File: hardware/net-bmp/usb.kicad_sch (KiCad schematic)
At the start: 8 parts, among them J1 USB_C_Receptacle_USB2.0, U2 USBLC6-2SC6

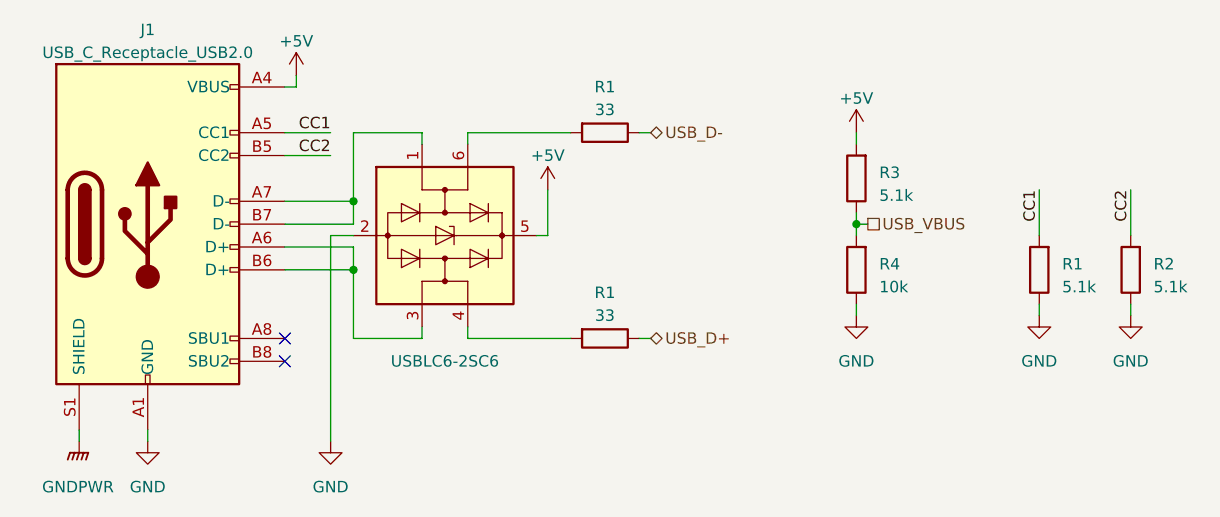
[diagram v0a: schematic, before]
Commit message: chore: build with stubs
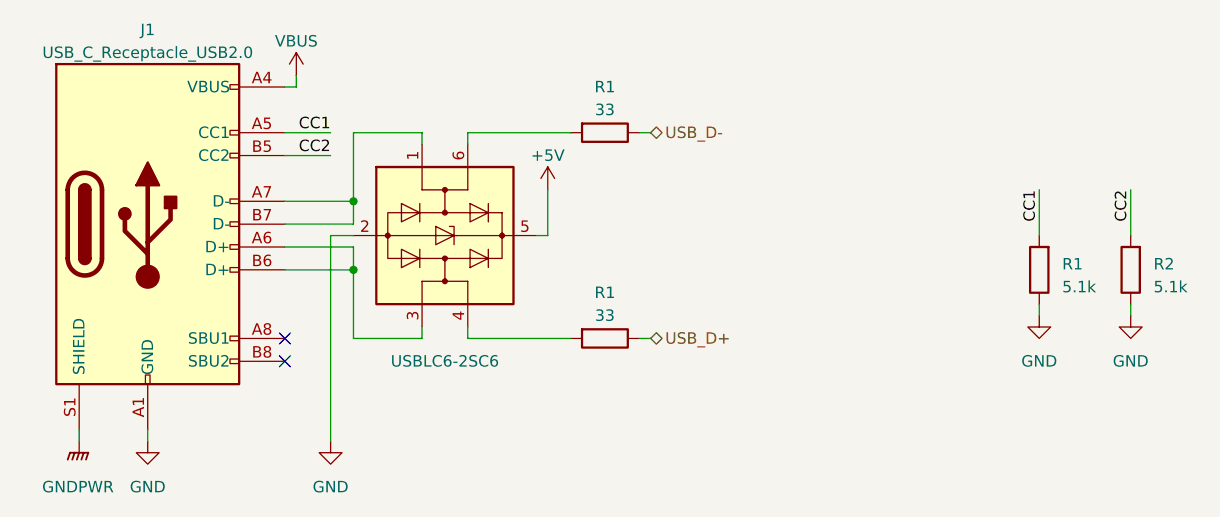
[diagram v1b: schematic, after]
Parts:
- removed R3: 5.1k, Resistor_SMD:R_0402_1005Metric, symbol Device:R
- removed R4: 10k, Resistor_SMD:R_0402_1005Metric, symbol Device:R
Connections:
- net +5V: no longer J1.A4 (VBUS), J1.A9 (VBUS), J1.B4 (VBUS), J1.B9 (VBUS)
- new net VBUS: J1.A4 (VBUS), J1.A9 (VBUS), J1.B4 (VBUS), J1.B9 (VBUS)
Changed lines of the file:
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@@
   (title_block
     (title "net-bmp")
-    (date "2023-10-31")
-    (rev "a")
+    (date "2023-11-11")
+    (rev "b")
     (company "elagil")
-  )
-  (junction (at 119.38 46.99) (diameter 0) (color 0 0 0 0)
   )
   (junction (at 63.5 44.45) (diameter 0) (color 0 0 0 0)
@@
     (stroke (width 0) (type default))
   )
-  (wire (pts (xy 119.38 36.83) (xy 119.38 38.1))
-    (stroke (width 0) (type default))
-  )
   (wire (pts (xy 149.86 55.88) (xy 149.86 57.15))
     (stroke (width 0) (type default))
@@
     (stroke (width 0) (type default))
   )
-  (wire (pts (xy 119.38 45.72) (xy 119.38 46.99))
-    (stroke (width 0) (type default))
-  )
   (wire (pts (xy 95.25 59.69) (xy 96.52 59.69))
     (stroke (width 0) (type default))
@@
     (stroke (width 0) (type default))
   )
-  (wire (pts (xy 119.38 46.99) (xy 119.38 48.26))
-    (stroke (width 0) (type default))
-  )
   (wire (pts (xy 55.88 31.75) (xy 57.15 31.75))
     (stroke (width 0) (type default))
   )
-  (wire (pts (xy 119.38 55.88) (xy 119.38 57.15))
-    (stroke (width 0) (type default))
-  )
   (wire (pts (xy 55.88 49.53) (xy 63.5 49.53))
-    (stroke (width 0) (type default))
-  )
-  (wire (pts (xy 119.38 46.99) (xy 120.65 46.99))
     (stroke (width 0) (type default))
   )
@@
     (effects (font (size 1.27 1.27)) (justify right bottom))
   )
-  (hierarchical_label "USB_VBUS" (shape passive) (at 120.65 46.99 0) (fields_autoplaced)
-    (effects (font (size 1.27 1.27)) (justify left))
-  )
   (hierarchical_label "USB_D+" (shape bidirectional) (at 96.52 59.69 0) (fields_autoplaced)
     (effects (font (size 1.27 1.27)) (justify left))
@@
   (hierarchical_label "USB_D-" (shape bidirectional) (at 96.52 36.83 0) (fields_autoplaced)
     (effects (font (size 1.27 1.27)) (justify left))
+  )
+  (symbol (lib_id "power:VBUS") (at 57.15 30.48 0) (unit 1)
+    (in_bom yes) (on_board yes) (dnp no)
+    (property "Reference" "#PWR067" (at 57.15 34.29 0)
+      (effects (font (size 1.27 1.27)) hide)
+    )
+    (property "Value" "VBUS" (at 57.15 26.67 0)
+      (effects (font (size 1.27 1.27)))
+    )
+    (property "Footprint" "" (at 57.15 30.48 0)
+      (effects (font (size 1.27 1.27)) hide)
+    )
+    (property "Datasheet" "" (at 57.15 30.48 0)
+      (effects (font (size 1.27 1.27)) hide)
+    )
+    (pin "1")
+    (instances
+      (project "net-bmp"
+        (path "/0556e588-02fe-48e5-93e8-fa3aab1c90e7/e157d64e-477b-4983-afb5-0491664aa612"
+          (reference "#PWR067") (unit 1)
+        )
+      )
+    )
   )
   (symbol (lib_id "Connector:USB_C_Receptacle_USB2.0") (at 40.64 46.99 0) (unit 1)
@@
     )
   )
-  (symbol (lib_id "power:+5V") (at 57.15 30.48 0) (unit 1)
-    (in_bom yes) (on_board yes) (dnp no) (fields_autoplaced)
-    (property "Reference" "#PWR08" (at 57.15 34.29 0)
-      (effects (font (size 1.27 1.27)) hide)
-    )
-    (property "Value" "+5V" (at 57.15 26.67 0)
-      (effects (font (size 1.27 1.27)))
-    )
-    (property "Footprint" "" (at 57.15 30.48 0)
-      (effects (font (size 1.27 1.27)) hide)
-    )
-    (property "Datasheet" "" (at 57.15 30.48 0)
-      (effects (font (size 1.27 1.27)) hide)
-    )
-    (pin "1")
-    (instances
-      (project "net-bmp"
-        (path "/0556e588-02fe-48e5-93e8-fa3aab1c90e7"
-          (reference "#PWR08") (unit 1)
-        )
-        (path "/0556e588-02fe-48e5-93e8-fa3aab1c90e7/e157d64e-477b-4983-afb5-0491664aa612"
-          (reference "#PWR064") (unit 1)
-        )
-      )
-    )
-  )
-  (symbol (lib_id "Device:R") (at 119.38 41.91 180) (unit 1)
-    (in_bom yes) (on_board yes) (dnp no) (fields_autoplaced)
-    (property "Reference" "R3" (at 121.92 41.275 0)
-      (effects (font (size 1.27 1.27)) (justify right))
-    )
-    (property "Value" "5.1k" (at 121.92 43.815 0)
-      (effects (font (size 1.27 1.27)) (justify right))
-    )
-    (property "Footprint" "Resistor_SMD:R_0402_1005Metric" (at 121.158 41.91 90)
-      (effects (font (size 1.27 1.27)) hide)
-    )
-    (property "Datasheet" "~" (at 119.38 41.91 0)
-      (effects (font (size 1.27 1.27)) hide)
-    )
-    (property "MPN" "C25905" (at 119.38 41.91 0)
-      (effects (font (size 1.27 1.27)) hide)
-    )
-    (property "JLCPCB Rotation Offset" "" (at 119.38 41.91 0)
-      (effects (font (size 1.27 1.27)) hide)
-    )
-    (pin "1")
-    (pin "2")
-    (instances
-      (project "net-bmp"
-        (path "/0556e588-02fe-48e5-93e8-fa3aab1c90e7"
-          (reference "R3") (unit 1)
-        )
-        (path "/0556e588-02fe-48e5-93e8-fa3aab1c90e7/e157d64e-477b-4983-afb5-0491664aa612"
-          (reference "R31") (unit 1)
-        )
-      )
-    )
-  )
-  (symbol (lib_id "Device:R") (at 119.38 52.07 180) (unit 1)
-    (in_bom yes) (on_board yes) (dnp no) (fields_autoplaced)
-    (property "Reference" "R4" (at 121.92 51.435 0)
-      (effects (font (size 1.27 1.27)) (justify right))
-    )
-    (property "Value" "10k" (at 121.92 53.975 0)
-      (effects (font (size 1.27 1.27)) (justify right))
-    )
-    (property "Footprint" "Resistor_SMD:R_0402_1005Metric" (at 121.158 52.07 90)
-      (effects (font (size 1.27 1.27)) hide)
-    )
-    (property "Datasheet" "~" (at 119.38 52.07 0)
-      (effects (font (size 1.27 1.27)) hide)
-    )
-    (property "MPN" "C25744" (at 119.38 52.07 0)
-      (effects (font (size 1.27 1.27)) hide)
-    )
-    (property "JLCPCB Rotation Offset" "" (at 119.38 52.07 0)
-      (effects (font (size 1.27 1.27)) hide)
-    )
-    (pin "1")
-    (pin "2")
-    (instances
-      (project "net-bmp"
-        (path "/0556e588-02fe-48e5-93e8-fa3aab1c90e7"
-          (reference "R4") (unit 1)
-        )
-        (path "/0556e588-02fe-48e5-93e8-fa3aab1c90e7/e157d64e-477b-4983-afb5-0491664aa612"
-          (reference "R32") (unit 1)
-        )
-      )
-    )
-  )
   (symbol (lib_id "power:GNDPWR") (at 33.02 71.12 0) (unit 1)
     (in_bom yes) (on_board yes) (dnp no) (fields_autoplaced)
@@
         )
       )
-    )
-  )
-  (symbol (lib_id "power:+5V") (at 119.38 36.83 0) (unit 1)
-    (in_bom yes) (on_board yes) (dnp no) (fields_autoplaced)
-    (property "Reference" "#PWR013" (at 119.38 40.64 0)
-      (effects (font (size 1.27 1.27)) hide)
-    )
-    (property "Value" "+5V" (at 119.38 33.02 0)
-      (effects (font (size 1.27 1.27)))
-    )
-    (property "Footprint" "" (at 119.38 36.83 0)
-      (effects (font (size 1.27 1.27)) hide)
-    )
-    (property "Datasheet" "" (at 119.38 36.83 0)
-      (effects (font (size 1.27 1.27)) hide)
-    )
-    (pin "1")
-    (instances
-      (project "net-bmp"
-        (path "/0556e588-02fe-48e5-93e8-fa3aab1c90e7"
-          (reference "#PWR013") (unit 1)
-        )
-        (path "/0556e588-02fe-48e5-93e8-fa3aab1c90e7/e157d64e-477b-4983-afb5-0491664aa612"
-          (reference "#PWR067") (unit 1)
-        )
-      )
-    )
-  )
-  (symbol (lib_id "power:GND") (at 119.38 57.15 0) (unit 1)
-    (in_bom yes) (on_board yes) (dnp no)
-    (property "Reference" "#PWR014" (at 119.38 63.5 0)
-      (effects (font (size 1.27 1.27)) hide)
-    )
-    (property "Value" "GND" (at 119.38 62.23 0)
-      (effects (font (size 1.27 1.27)))
-    )
-    (property "Footprint" "" (at 119.38 57.15 0)
-      (effects (font (size 1.27 1.27)) hide)
-    )
-    (property "Datasheet" "" (at 119.38 57.15 0)
-      (effects (font (size 1.27 1.27)) hide)
-    )
-    (pin "1")
-    (instances
-      (project "net-bmp"
-        (path "/0556e588-02fe-48e5-93e8-fa3aab1c90e7"
-          (reference "#PWR014") (unit 1)
-        )
-        (path "/0556e588-02fe-48e5-93e8-fa3aab1c90e7/e157d64e-477b-4983-afb5-0491664aa612"
-          (reference "#PWR068") (unit 1)
-        )
-      )
